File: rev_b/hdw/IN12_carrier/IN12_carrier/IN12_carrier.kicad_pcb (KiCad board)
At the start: 2 copper layers, 205 x 50 mm, 208 parts, among them Q401 MMSTA42, Q402 MMSTA42, Q403 MMSTA42, Q404 MMSTA92, Q405 MMSTA92, Q406 MMSTA92, Q407 MMSTA42, Q408 MMSTA42, Q409 MMSTA42, Q410 MMSTA92, Q411 MMSTA92, Q412 MMSTA92, Q501 MMSTA42, Q502 MMSTA42, Q503 MMSTA42, Q504 MMSTA42, Q505 MMSTA42, Q506 MMSTA42, Q507 MMSTA42, Q508 MMSTA42, Q509 MMSTA42, Q510 MMSTA42, Q511 MMSTA42, Q512 MMSTA42, Q513 MMSTA42, SW901 Cap_Touch, SW902 Cap_Touch, SW903 Cap_Touch, SW904 Cap_Touch, SW905 Cap_Touch, U1001 TCA9555RGER, U1002 24AA02-OT, U1101 MAX6818, U301 DS1683, U302 LTC4316DD, U701 LP5009, U702 LP5009, U703 LP5009, U901 AT42QT1010-TSHR, U902 AT42QT1010-TSHR, U903 AT42QT1010-TSHR, U904 AT42QT1010-TSHR, U905 74LVC1G17, U906 74LVC1G17, U907 74LVC1G17, U908 74LVC1G17, U909 AT42QT1010-TSHR, U910 74LVC1G17

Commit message: lots of placement progress on IN12 carrier board
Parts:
- removed R702, R703: 10k, Resistors_SMD:R_0603
- added C1101: 0.1uF, Capacitors_SMD:C_0603, F.Cu at (75.6, 182.9)
- added H1201: MountingHole, MountingHole:MountingHole_3mm, F.Cu at (38.3, 129.3)
- added H1202: MountingHole, MountingHole:MountingHole_3mm, F.Cu at (38.3, 85.3)
- added H1203: MountingHole, MountingHole:MountingHole_3mm, F.Cu at (101.9, 85.3)
- added H1204: MountingHole, MountingHole:MountingHole_3mm, F.Cu at (101.9, 129.3)
- added H1205: MountingHole, MountingHole:MountingHole_3mm, F.Cu at (168.6, 85.3)
- added H1206: MountingHole, MountingHole:MountingHole_3mm, F.Cu at (168.6, 129.3)
- added H1207: MountingHole, MountingHole:MountingHole_3mm, F.Cu at (232.3, 85.3)
- added H1208: MountingHole, MountingHole:MountingHole_3mm, F.Cu at (232.3, 129.3)
- added J1101: Power, Connector_PinHeader_2.54mm:PinHeader_1x02_P2.54mm_Vertical, F.Cu at (66.3, 180.4)
- added J1102: Left, Connector_PinHeader_2.54mm:PinHeader_1x02_P2.54mm_Vertical, F.Cu at (66.3, 185.0)
- added J1103: Right, Connector_PinHeader_2.54mm:PinHeader_1x02_P2.54mm_Vertical, F.Cu at (66.3, 189.7)
- added J1104: Up, Connector_PinHeader_2.54mm:PinHeader_1x02_P2.54mm_Vertical, F.Cu at (66.3, 194.3)
- added J1105: Down, Connector_PinHeader_2.54mm:PinHeader_1x02_P2.54mm_Vertical, F.Cu at (66.3, 199.0)
- added J201: Conn_02x32_Top_Bottom, Custom Footprints Library:CONN_5120528-1_TYC, B.Cu at (233.2, 91.9)
- added Q514: MMSTA42, TO_SOT_Packages_SMD:SOT-323_SC-70, F.Cu at (63.0, 162.6)
- added Q515: MMSTA42, TO_SOT_Packages_SMD:SOT-323_SC-70, F.Cu at (63.0, 159.4)
- added R201: 499, Resistors_SMD:R_0603, B.Cu at (226.6, 115.8)
- added R515: 10k, Resistors_SMD:R_0603, F.Cu at (60.5, 162.6)
- added R516: 10k, Resistors_SMD:R_0603, F.Cu at (60.5, 159.4)
- added R603: 10k, Resistors_SMD:R_0805, B.Cu at (163.8, 103.2)
- added R604: 10k, Resistors_SMD:R_0805, B.Cu at (163.8, 111.5)
- added V606: IN3, LED_THT:LED_D5.0mm, F.Cu at (100.7, 103.2)
- added V607: IN3, LED_THT:LED_D5.0mm, F.Cu at (100.7, 111.5)
- added V609: IN3, LED_THT:LED_D5.0mm, F.Cu at (167.3, 103.2)
- added V610: IN3, LED_THT:LED_D5.0mm, F.Cu at (167.3, 111.5)
- C1001, R601, R602, U1002: moved to B.Cu
- moved R511 469.5 mm to (40.3, 177.6), turned to 90 degrees
- moved R514 456.8 mm to (45.6, 177.6), turned to -90 degrees
- moved Q511 455.9 mm to (42.8, 177.6)
- moved R512 448.5 mm to (60.5, 156.2), turned to 90 degrees
- moved R513 448.4 mm to (60.5, 153.0), turned to 90 degrees
- moved D301 443.0 mm to (119.7, 161.8), turned to -90 degrees
- moved U301 440.3 mm to (122.8, 166.3)
- moved C301 435.2 mm to (121.4, 161.8), turned to 90 degrees
- moved Q513 434.8 mm to (63.0, 153.0)
- moved Q512 434.8 mm to (63.0, 156.2)
- moved C302 433.5 mm to (122.8, 161.8), turned to 90 degrees
- moved R302 432.2 mm to (127.3, 165.1), turned to -90 degrees
- moved U302 432.2 mm to (132.1, 166.2), turned to 180 degrees
- moved C303 431.9 mm to (124.1, 161.8), turned to 90 degrees
- moved R301 431.0 mm to (128.9, 165.1), turned to -90 degrees
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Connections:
- R401 pad 1: Anode_Drive_0 -> Anode_0_DSP
- R402 pad 1: Anode_Drive_2 -> Anode_2_DSP
- R403 pad 1: Anode_Drive_4 -> Anode_4_DSP
- R413 pad 1: Anode_Drive_1 -> Anode_1_DSP
- R414 pad 1: Anode_Drive_3 -> Anode_3_DSP
- R415 pad 1: Anode_Drive_5 -> Anode_5_DSP
- R501 pad 1: Cathode_Drive_0 -> Cathode_0_DSP
- R502 pad 1: Cathode_Drive_2 -> Cathode_2_DSP
- R503 pad 1: Cathode_Drive_4 -> Cathode_4_DSP
- R504 pad 1: Cathode_Drive_6 -> Cathode_6_DSP
- R505 pad 1: Cathode_Drive_8 -> Cathode_8_DSP
- R506 pad 1: Cathode_Drive_1 -> Cathode_1_DSP
- R507 pad 1: Cathode_Drive_3 -> Cathode_3_DSP
- R508 pad 1: Cathode_Drive_5 -> Cathode_5_DSP
- R509 pad 1: Cathode_Drive_7 -> Cathode_7_DSP
- R510 pad 1: Cathode_Drive_9 -> Cathode_9_DSP
- R511 pad 1: Cathode_Drive_DP -> Cathode_DP_DSP
- U1101 pad 1: unconnected-(U1101-~{EN}-Pad1) -> GND
- U1101 pad 10: unconnected-(U1101-GND-Pad10) -> GND
- U1101 pad 15: unconnected-(U1101-OUT5-Pad15) -> Pushbutton_Down
- U1101 pad 16: unconnected-(U1101-OUT4-Pad16) -> Pushbutton_Up
- U1101 pad 17: unconnected-(U1101-OUT3-Pad17) -> Pushbutton_Right
- U1101 pad 18: unconnected-(U1101-OUT2-Pad18) -> Pushbutton_Left
- U1101 pad 19: unconnected-(U1101-OUT1-Pad19) -> Pushbutton_Power
- U1101 pad 2: unconnected-(U1101-IN1-Pad2) -> Net-(J1101-Pin_1)
- U1101 pad 20: unconnected-(U1101-VCC-Pad20) -> +3.3V
- U1101 pad 3: unconnected-(U1101-IN2-Pad3) -> Net-(J1102-Pin_1)
- U1101 pad 4: unconnected-(U1101-IN3-Pad4) -> Net-(J1103-Pin_1)
- U1101 pad 5: unconnected-(U1101-IN4-Pad5) -> Net-(J1104-Pin_1)
- U1101 pad 6: unconnected-(U1101-IN5-Pad6) -> Net-(J1105-Pin_1)
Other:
- board size 205 x 50 mm -> 200 x 50 mm
- board text added: "To-Do: * Double check LED clearance from IN-12 hole * Check to see if IN12 footprint needs a hole * Double check IN12 pinout * Double check IN12 PTH drill size * Stackup legend * Stackup table * Owl * Board name * Board date * Board stats"

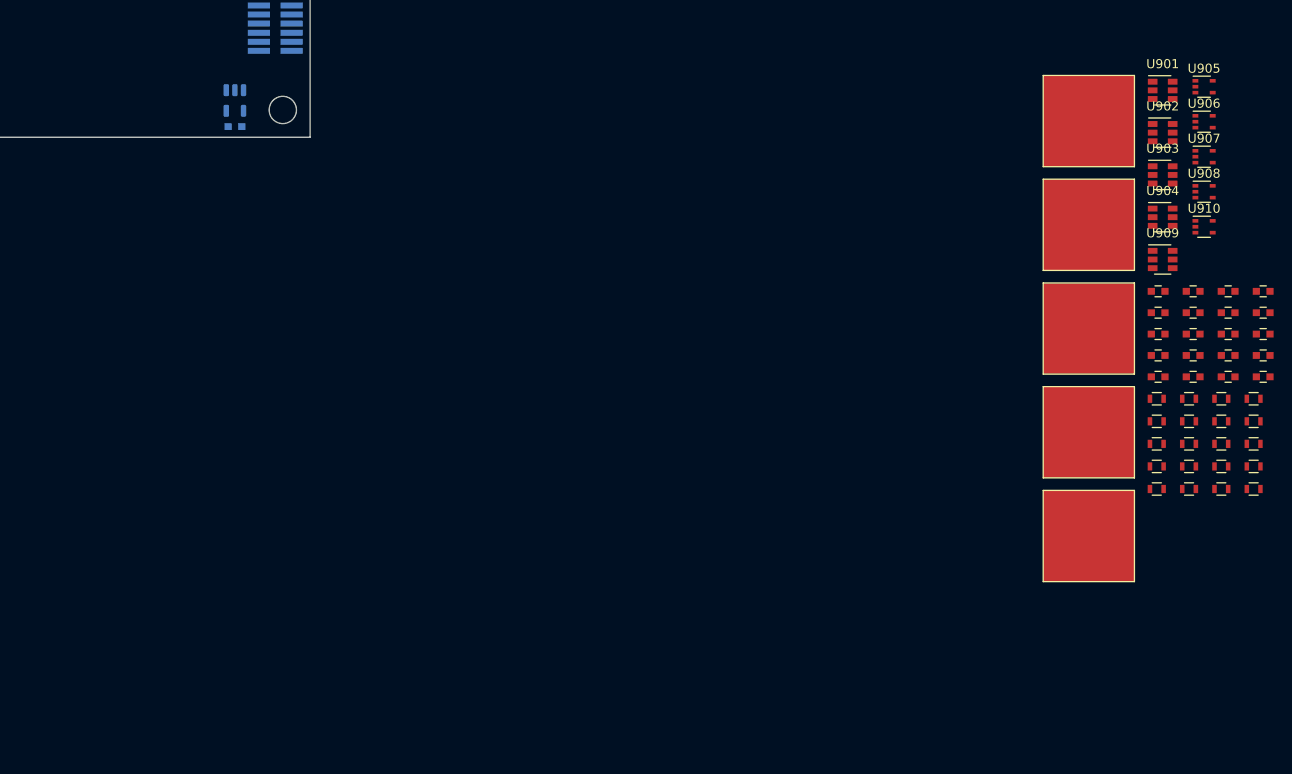
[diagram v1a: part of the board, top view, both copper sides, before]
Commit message: lots more IN12 carrier placement
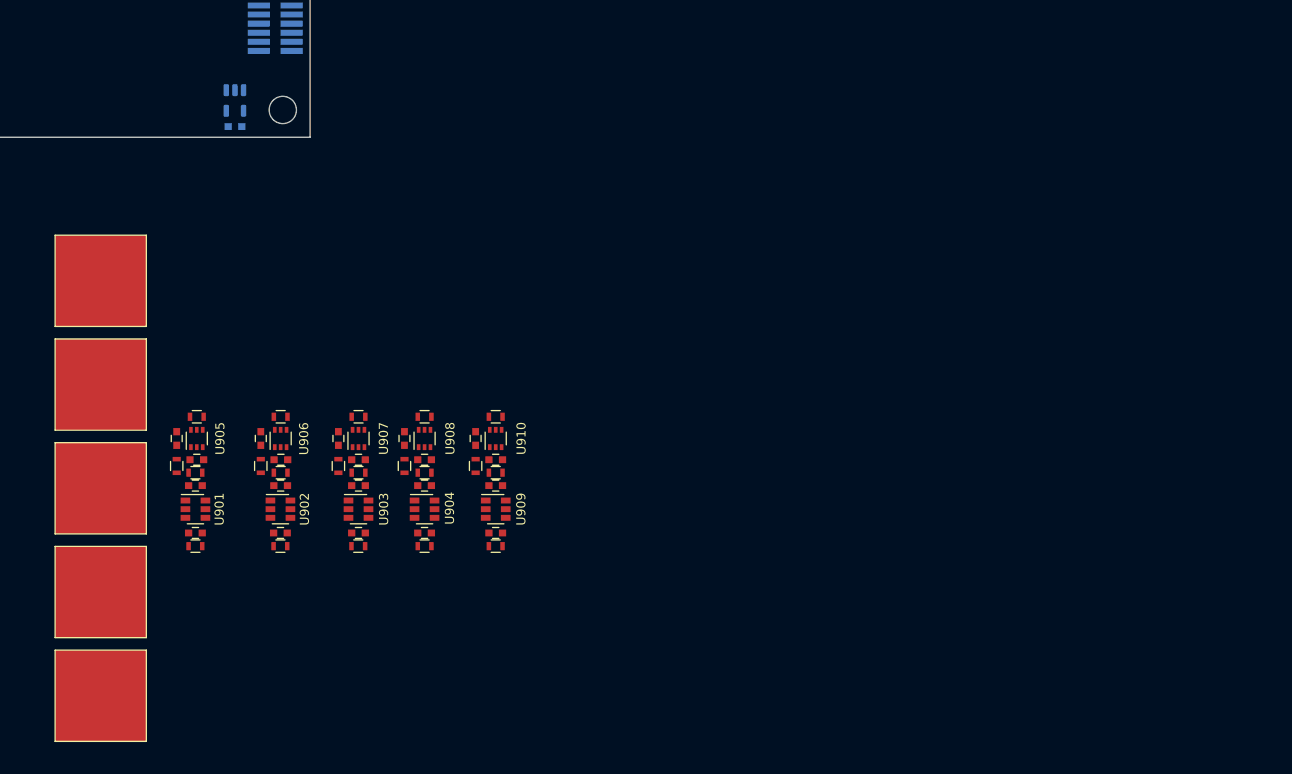
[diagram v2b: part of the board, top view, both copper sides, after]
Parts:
- U905, U906, U907, U908, U910: value 74LVC1G17 -> 74LVC1G97; footprint TO_SOT_Packages_SMD:SOT-353_SC-70-5 -> Package_TO_SOT_SMD:SOT-363_SC-70-6
- moved U905 117.3 mm to (222.8, 165.5), turned to 90 degrees
- moved C913 116.2 mm to (220.6, 165.5), turned to -90 degrees
- moved U901 115.9 mm to (222.7, 173.2)
- moved R913 112.7 mm to (222.8, 163.1), turned to 180 degrees
- moved R909 111.3 mm to (220.6, 168.5), turned to -90 degrees
- moved C909 110.2 mm to (222.8, 167.8)
- moved SW901 110.1 mm to (212.2, 148.1)
- moved SW902 110.1 mm to (212.2, 159.5)
- moved SW903 110.1 mm to (212.2, 170.9)
- moved SW904 110.1 mm to (212.2, 182.4)
- moved SW905 110.1 mm to (212.2, 193.8)
- moved C901 109.1 mm to (222.7, 175.9), turned to 180 degrees
- moved U906 107.3 mm to (232.0, 165.5), turned to 90 degrees
- moved R901 106.9 mm to (222.7, 177.3), turned to 180 degrees
- moved C914 106.8 mm to (229.8, 165.5), turned to -90 degrees
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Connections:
- U905 pad 1: (no net) -> Net-(C909-Pad1)
- U905 pad 2: Net-(C909-Pad1) -> GND
- U906 pad 1: (no net) -> Net-(C910-Pad1)
- U906 pad 2: Net-(C910-Pad1) -> GND
- U907 pad 1: (no net) -> Net-(C911-Pad1)
- U907 pad 2: Net-(C911-Pad1) -> GND
- U908 pad 1: (no net) -> Net-(C912-Pad1)
- U908 pad 2: Net-(C912-Pad1) -> GND
- U910 pad 1: (no net) -> Net-(C919-Pad1)
- U910 pad 2: Net-(C919-Pad1) -> GND

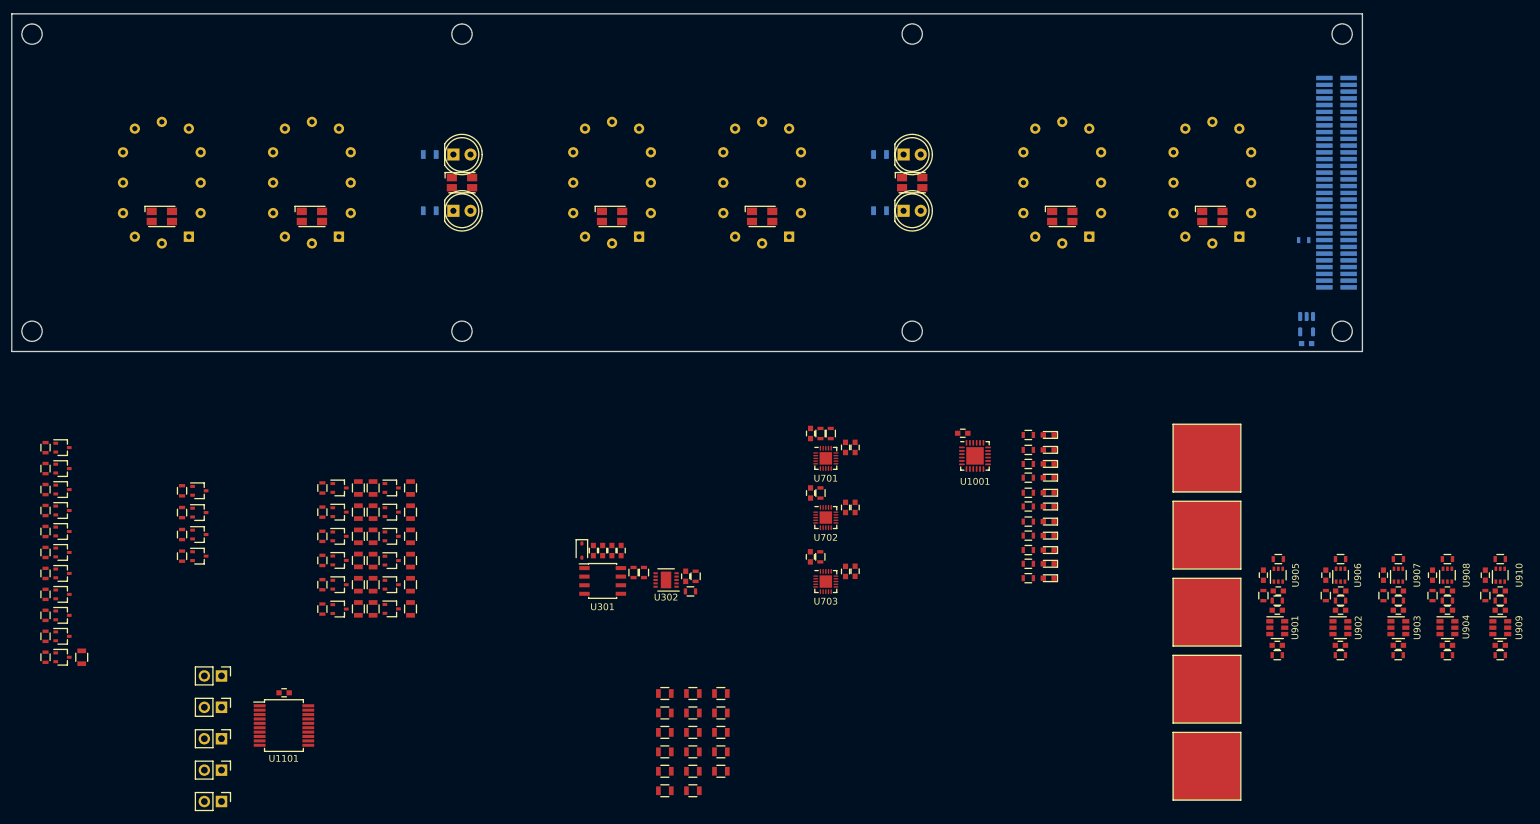
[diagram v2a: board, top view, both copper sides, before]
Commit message: lots of routing and design progress on IN12 carrier board
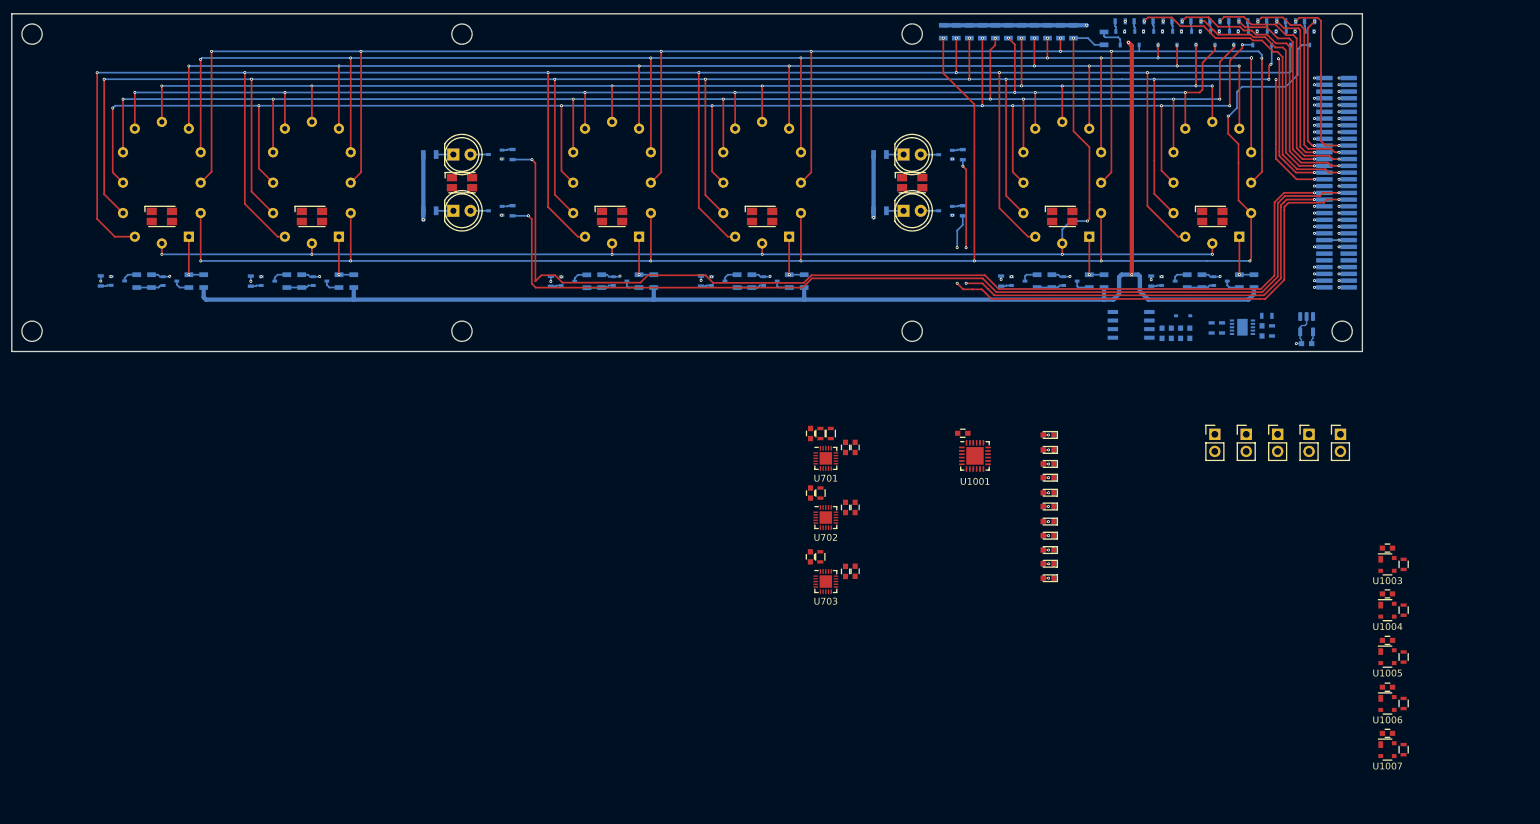
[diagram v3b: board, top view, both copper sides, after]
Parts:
- removed C1101, C905, C906, C907, C908, C913, C914, C915, C916, C918, C920: 0.1uF, Capacitors_SMD:C_0603
- removed C901, C902, C903, C904, C917: 10nF, Capacitors_SMD:C_0603
- removed C909, C910, C911, C912, C919: 10uF, Capacitors_SMD:C_0603
- removed R201, R901, R902, R903, R904, R917: 499, Resistors_SMD:R_0603
- removed R905, R906, R907, R908, R909, R910, R911, R912, R913, R914, R915, R916, R918, R919, R920: 10k, Resistors_SMD:R_0603
- removed SW901, SW902, SW903, SW904, SW905: Cap_Touch, Custom Footprints Library:Capacitive_Touch_Pad
- removed U1101: MAX6818, Housings_SSOP:SSOP-20_5.3x7.2mm_Pitch0.65mm
- removed U901, U902, U903, U904, U909: AT42QT1010-TSHR, TO_SOT_Packages_SMD:SOT-23-6
- removed U905, U906, U907, U908, U910: 74LVC1G97, Package_TO_SOT_SMD:SOT-363_SC-70-6
- added C1003: 0.1uF, Capacitors_SMD:C_0603, F.Cu at (239.0, 161.5)
- added C1004: 0.1uF, Capacitors_SMD:C_0603, F.Cu at (239.0, 168.2)
- added C1005: 0.1uF, Capacitors_SMD:C_0603, F.Cu at (239.0, 175.1)
- added C1006: 0.1uF, Capacitors_SMD:C_0603, F.Cu at (239.0, 182.1)
- added C1007: 0.1uF, Capacitors_SMD:C_0603, F.Cu at (239.0, 188.9)
- added R1012: 10k, Resistors_SMD:R_0603, F.Cu at (241.4, 163.9)
- added R1013: 10k, Resistors_SMD:R_0603, F.Cu at (241.4, 170.6)
- added R1014: 10k, Resistors_SMD:R_0603, F.Cu at (241.4, 177.6)
- added R1015: 10k, Resistors_SMD:R_0603, F.Cu at (241.4, 184.5)
- added R1016: 10k, Resistors_SMD:R_0603, F.Cu at (241.4, 191.3)
- added U1003: MAX6816, Package_TO_SOT_SMD:SOT-143, F.Cu at (239.0, 163.9)
- added U1004: MAX6816, Package_TO_SOT_SMD:SOT-143, F.Cu at (239.0, 170.6)
- added U1005: MAX6816, Package_TO_SOT_SMD:SOT-143, F.Cu at (239.0, 177.5)
- added U1006: MAX6816, Package_TO_SOT_SMD:SOT-143, F.Cu at (239.0, 184.5)
- added U1007: MAX6816, Package_TO_SOT_SMD:SOT-143, F.Cu at (239.0, 191.3)
- C301, C302, C303, C304, C305, D301, Q401, Q402, Q403, Q404, Q405, Q406, Q407, Q408, Q409, Q410, Q411, Q412, Q501, Q502, Q503, Q504, Q505, Q506, Q507, Q508, Q509, Q510, Q511, Q512, Q513, Q514, Q515, R1001, R1002, R1003, R1004, R1005, R1006, R1007, R1008, R1009, R1010, R1011, R301, R302, R303, R304, R401, R402, R403, R404, R405, R406, R407, R408, R409, R410, R411, R412, R413, R414, R415, R416, R417, R418, R419, R420, R421, R422, R423, R424, R501, R502, R503, R504, R505, R506, R507, R508, R509, R510, R511, R512, R513, R514, R515, R516, R801, R802, R803, R804, R805, R806, R807, R808, R809, R810, R811, R812, R813, R814, R815, R816, R817, U301, U302: moved to B.Cu
- moved R501 197.5 mm to (227.4, 83.4), turned to 180 degrees
- moved R506 195.9 mm to (224.6, 83.4), turned to 180 degrees
- moved R502 194.4 mm to (221.8, 83.4), turned to 180 degrees
- moved Q501 194.4 mm to (227.4, 86.0), turned to -90 degrees
- moved R507 192.9 mm to (219.0, 83.4), turned to 180 degrees
- moved Q506 192.7 mm to (224.6, 86.0), turned to -90 degrees
- moved R503 191.5 mm to (216.2, 83.4), turned to 180 degrees
- moved Q502 191.1 mm to (221.8, 86.0), turned to -90 degrees
- moved R508 190.2 mm to (213.4, 83.4), turned to 180 degrees
- moved Q507 189.6 mm to (219.0, 86.0), turned to -90 degrees
- moved R504 189.0 mm to (210.6, 83.4), turned to 180 degrees
- moved Q503 188.2 mm to (216.2, 86.0), turned to -90 degrees
- moved R509 187.8 mm to (207.8, 83.4), turned to 180 degrees
- moved Q508 186.9 mm to (213.4, 86.0), turned to -90 degrees
- moved R505 186.8 mm to (205.0, 83.4), turned to 180 degrees
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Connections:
- C704 pad 1: +3V3 -> +3.3V
- C705 pad 1: +3V3 -> +3.3V
- C706 pad 1: +3V3 -> +3.3V
- C707 pad 1: +3V3 -> +3.3V
- C708 pad 1: +3V3 -> +3.3V
- C709 pad 1: +3V3 -> +3.3V
- D701 pad 1: +3V3 -> +3.3V
- D702 pad 1: +3V3 -> +3.3V
- D703 pad 1: +3V3 -> +3.3V
- D704 pad 1: +3V3 -> +3.3V
- D705 pad 1: +3V3 -> +3.3V
- D706 pad 1: +3V3 -> +3.3V
- D707 pad 1: +3V3 -> +3.3V
- D708 pad 1: +3V3 -> +3.3V
- J201 pad 21: Pushbutton_1_DSP -> Pushbutton_Left
- J201 pad 22: Pushbutton_3_DSP -> Pushbutton_Up
- J201 pad 23: Pushbutton_5_DSP -> unconnected-(J201-Pin_23-Pad23)
- J201 pad 53: Pushbutton_0_DSP -> Pushbutton_Power
- J201 pad 54: Pushbutton_2_DSP -> Pushbutton_Right
- J201 pad 55: Pushbutton_4_DSP -> Pushbutton_Down
- J201 pad 56: Pushbutton_6_DSP -> unconnected-(J201-Pin_56-Pad56)
- J201 pad 57: ~{Display_Detect_DSP} -> GND
- U701 pad 16: +3V3 -> +3.3V
- U702 pad 14: +3V3 -> +3.3V
- U702 pad 16: +3V3 -> +3.3V
- U703 pad 15: +3V3 -> +3.3V
- U703 pad 16: +3V3 -> +3.3V
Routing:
- net Cathode_1: track 0.00 -> 350.3 mm, vias 0 -> 8
- net Cathode_2: track 0.00 -> 309.7 mm, vias 0 -> 10
- net Cathode_9: track 0.00 -> 278.7 mm, vias 0 -> 8
- net +90V: track 0.00 -> 269.5 mm, vias 0 -> 5
- net Cathode_0: track 0.00 -> 268.7 mm, vias 0 -> 9
- net Cathode_3: track 0.00 -> 259.3 mm, vias 0 -> 10
- net +180V: track 0.00 -> 253.2 mm, vias 0 -> 10
- net Cathode_8: track 0.00 -> 244.2 mm, vias 0 -> 11
- net Cathode_4: track 0.00 -> 227.9 mm, vias 0 -> 10
- net Cathode_7: track 0.00 -> 218.4 mm, vias 0 -> 10
- net Anode_5_DSP: track 0.00 -> 207.1 mm, vias 0 -> 2
- net Cathode_5: track 0.00 -> 206.2 mm, vias 0 -> 9
- net Cathode_DP: track 0.00 -> 204.7 mm, vias 0 -> 8
- net Cathode_6: track 0.00 -> 200.7 mm, vias 0 -> 10
- net Anode_4_DSP: track 0.00 -> 181.0 mm, vias 0 -> 2
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- added copper zone on In2.Cu, net GND
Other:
- copper layers 2 -> 4

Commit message: carrier board layout progress
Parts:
- C1003, C1004, C1005, C1006, C1007, R1012, R1013, R1014, R1015, R1016, U1003, U1004, U1005, U1006, U1007: moved to B.Cu
- moved R1016 226.6 mm to (37.3, 92.8)
- moved C1007 222.4 mm to (39.6, 90.4), turned to 0 degrees
- moved U1007 222.4 mm to (39.6, 92.8), turned to 180 degrees
- moved R1014 216.0 mm to (37.3, 106.9)
- moved R1012 213.9 mm to (37.3, 99.8)
- moved R1015 213.7 mm to (37.3, 121.0)
- moved R1013 211.8 mm to (37.3, 113.9)
- moved C1005 211.5 mm to (39.6, 104.4), turned to 0 degrees
- moved U1005 211.5 mm to (39.6, 106.9), turned to 180 degrees
- moved C1003 209.4 mm to (39.6, 97.4), turned to 0 degrees
- moved U1003 209.4 mm to (39.6, 99.8), turned to 180 degrees
- moved C1006 209.2 mm to (39.6, 118.6), turned to 0 degrees
- moved U1006 209.2 mm to (39.6, 121.0), turned to 180 degrees
- moved C1004 207.2 mm to (39.6, 111.5), turned to 0 degrees
- moved U1004 207.2 mm to (39.6, 113.9), turned to 180 degrees
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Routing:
- net Net-(J1105-Pin_1): track 0.00 -> 90.1 mm
- net Net-(J1104-Pin_1): track 0.00 -> 70.8 mm
- net Net-(J1103-Pin_1): track 0.00 -> 51.4 mm
- net Net-(J1102-Pin_1): track 0.00 -> 32.8 mm
- net +3.3V: track 7.54 -> 22.8 mm
- net Net-(J1101-Pin_1): track 0.00 -> 13.9 mm
- net GND: track 34.9 -> 47.5 mm, vias 41 -> 46
- net Pushbutton_Up: track 1.43 -> 2.90 mm
- net Pushbutton_Down: track 1.43 -> 2.90 mm
- net Pushbutton_Power: track 1.43 -> 2.90 mm
- net Pushbutton_Left: track 1.43 -> 2.90 mm
- net Pushbutton_Right: track 1.43 -> 2.88 mm
- net Colon_0_DSP: track 153.2 -> 154.0 mm
- net Colon_1_DSP: track 147.7 -> 148.4 mm
